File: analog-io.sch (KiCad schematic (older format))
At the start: 88 parts, among them Q1001 BSS308, U1001 AD7294BSUZ, X1001 SMB, X1002 SMB, X1003 SMB, X1004 SMB, X1005 SMB, X1006 SMB, X1007 SMB, X1008 SMB, X1009 SMB, X1010 SMB, X1011 SMB, X1012 SMB

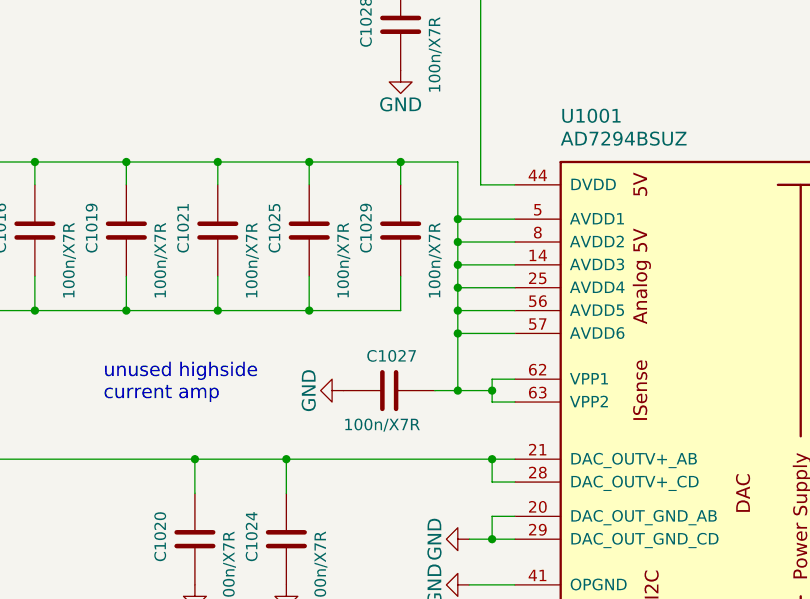
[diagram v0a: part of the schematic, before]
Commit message: fixed missing Rs before Potis - fixed (removed) AD7294 Vpp connection
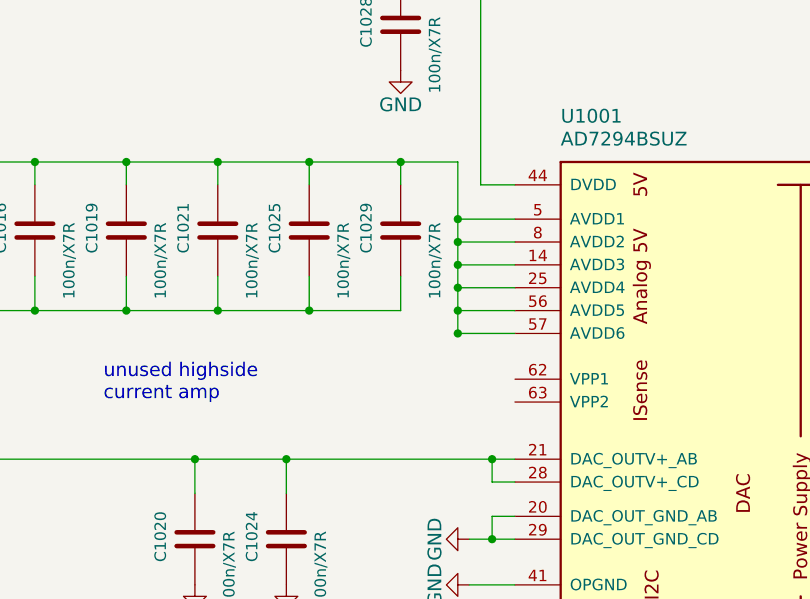
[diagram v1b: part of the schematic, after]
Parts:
- removed C1027: 100n/X7R, Capacitors_SMD:C_0603, symbol C
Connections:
- net +5VA: no longer U1001.62 (VPP1), U1001.63 (VPP2)

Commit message: Rev B. Layout - Gerber/BOM need to be reexported
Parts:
- C1001, C1002: value 100n/X7R -> 1n/X7R
- C1005, C1007, C1011, C1014: value 100n/X7R -> 100p/X7R
